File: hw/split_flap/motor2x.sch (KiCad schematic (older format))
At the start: 5 parts, among them J10 Conn_01x05, J9 Conn_01x05, U4 ULN2803A, U9 74HC595

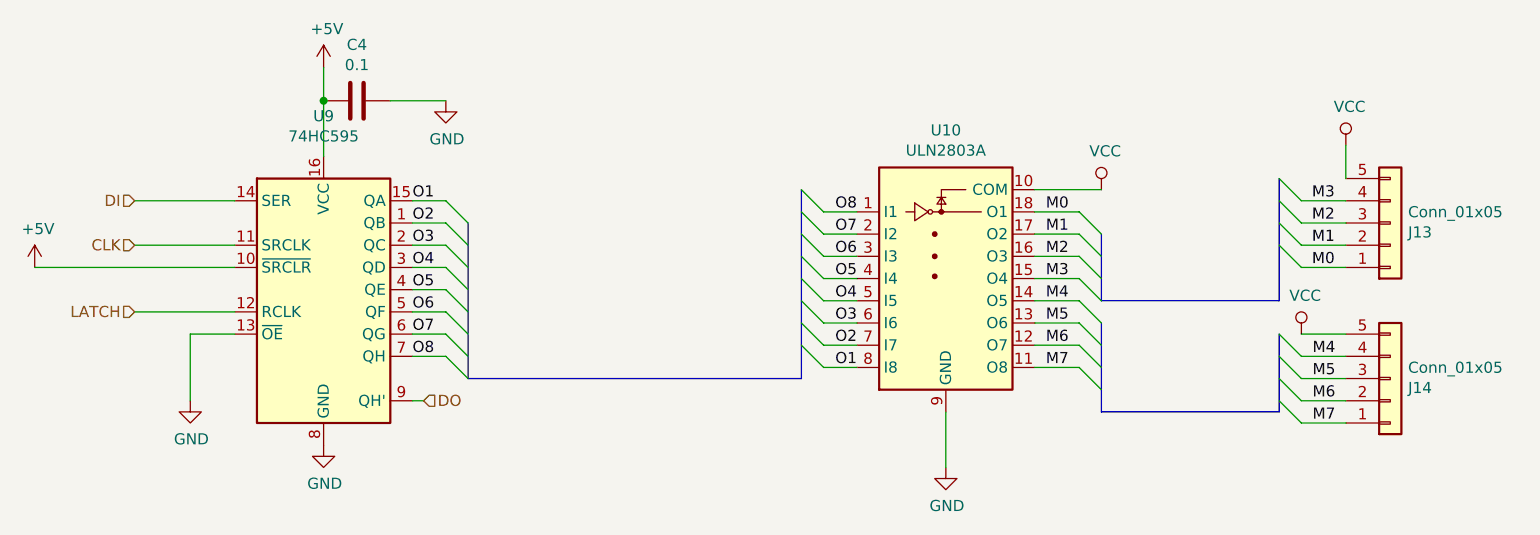
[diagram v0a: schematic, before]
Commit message: Add i2c pullups
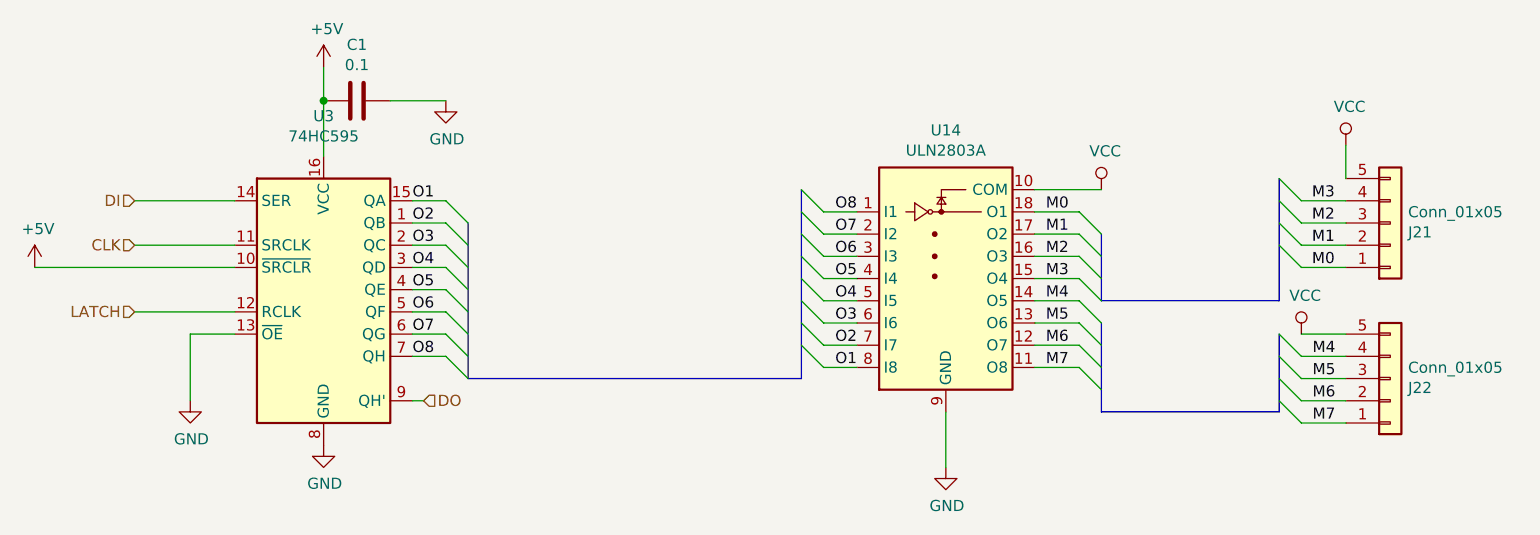
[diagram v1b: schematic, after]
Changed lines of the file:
@@
 AR Path="/5E0964A4/5E0DEDAF" Ref="#PWR033"  Part="1"
 AR Path="/5E0B21A0/5E0DEDAF" Ref="#PWR051"  Part="1"
-F 0 "#PWR051" H 4850 3850 50  0001 C CNN
+F 0 "#PWR0159" H 4850 3850 50  0001 C CNN
 F 1 "GND" H 4855 3927 50  0000 C CNN
 F 2 "" H 4850 4100 50  0001 C CNN
@@
 AR Path="/5E0964A4/5DF98B62" Ref="#PWR032"  Part="1"
 AR Path="/5E0B21A0/5DF98B62" Ref="#PWR050"  Part="1"
-F 0 "#PWR050" H 4850 2250 50  0001 C CNN
+F 0 "#PWR012" H 4850 2250 50  0001 C CNN
 F 1 "+5V" H 4865 2573 50  0000 C CNN
 F 2 "" H 4850 2400 50  0001 C CNN
@@
 AR Path="/5E0964A4/5DF9B643" Ref="#PWR031"  Part="1"
 AR Path="/5E0B21A0/5DF9B643" Ref="#PWR049"  Part="1"
-F 0 "#PWR049" H 4250 3650 50  0001 C CNN
+F 0 "#PWR011" H 4250 3650 50  0001 C CNN
 F 1 "GND" H 4255 3727 50  0000 C CNN
 F 2 "" H 4250 3900 50  0001 C CNN
@@
 AR Path="/5E0964A4/5DF9D02C" Ref="#PWR030"  Part="1"
 AR Path="/5E0B21A0/5DF9D02C" Ref="#PWR048"  Part="1"
-F 0 "#PWR048" H 3550 3150 50  0001 C CNN
+F 0 "#PWR08" H 3550 3150 50  0001 C CNN
 F 1 "+5V" H 3565 3473 50  0000 C CNN
 F 2 "" H 3550 3300 50  0001 C CNN
@@
 AR Path="/5E092C79/5E0E710C" Ref="C3"  Part="1"
 AR Path="/5E0B21A0/5E0E710C" Ref="C4"  Part="1"
-F 0 "C4" V 5252 2550 50  0000 C CNN
+F 0 "C1" V 5252 2550 50  0000 C CNN
 F 1 "0.1" V 5161 2550 50  0000 C CNN
 F 2 "Capacitor_THT:C_Disc_D4.3mm_W1.9mm_P5.00mm" H 5038 2400 50  0001 C CNN
@@
 AR Path="/5E0964A4/5E0E7881" Ref="#PWR034"  Part="1"
 AR Path="/5E0B21A0/5E0E7881" Ref="#PWR052"  Part="1"
-F 0 "#PWR052" H 5400 2300 50  0001 C CNN
+F 0 "#PWR013" H 5400 2300 50  0001 C CNN
 F 1 "GND" H 5405 2377 50  0000 C CNN
 F 2 "" H 5400 2550 50  0001 C CNN
@@
 AR Path="/5E0964A4/5DF4397F" Ref="U5"  Part="1"
 AR Path="/5E092C79/5DF4397F" Ref="U7"  Part="1"
-F 0 "U9" H 4850 4181 50  0000 C CNN
+F 0 "U3" H 4850 4181 50  0000 C CNN
 F 1 "74HC595" H 4850 4090 50  0000 C CNN
 F 2 "Package_SO:SOP-16_4.55x10.3mm_P1.27mm" H 4850 3400 50  0001 C CNN
@@
 AR Path="/5E0964A4/5E0DED94" Ref="J10"  Part="1"
 AR Path="/5E0B21A0/5E0DED94" Ref="J14"  Part="1"
-F 0 "J14" H 9730 3842 50  0000 L CNN
+F 0 "J22" H 9730 3842 50  0000 L CNN
 F 1 "Conn_01x05" H 9730 3751 50  0000 L CNN
 F 2 "Connector_JST:JST_XH_B5B-XH-A_1x05_P2.50mm_Vertical" H 9650 3800 50  0001 C CNN
@@
 AR Path="/5E0964A4/5E0DEDB5" Ref="#PWR035"  Part="1"
 AR Path="/5E0B21A0/5E0DEDB5" Ref="#PWR053"  Part="1"
-F 0 "#PWR053" H 7650 3950 50  0001 C CNN
+F 0 "#PWR0160" H 7650 3950 50  0001 C CNN
 F 1 "GND" H 7655 4027 50  0000 C CNN
 F 2 "" H 7650 4200 50  0001 C CNN
@@
 AR Path="/5E0964A4/5E0DEDBB" Ref="J9"  Part="1"
 AR Path="/5E0B21A0/5E0DEDBB" Ref="J13"  Part="1"
-F 0 "J13" H 9730 3142 50  0000 L CNN
+F 0 "J21" H 9730 3142 50  0000 L CNN
 F 1 "Conn_01x05" H 9730 3051 50  0000 L CNN
 F 2 "Connector_JST:JST_XH_B5B-XH-A_1x05_P2.50mm_Vertical" H 9650 3100 50  0001 C CNN
@@
 AR Path="/5E0964A4/5E0DEDCB" Ref="U6"  Part="1"
 AR Path="/5E0B21A0/5E0DEDCB" Ref="U10"  Part="1"
-F 0 "U10" H 7650 3817 50  0000 C CNN
+F 0 "U14" H 7650 3817 50  0000 C CNN
 F 1 "ULN2803A" H 7650 3726 50  0000 C CNN
 F 2 "Package_SO:SOP-18_7x12.5mm_P1.27mm" H 7700 2600 50  0001 L CNN
@@
 AR Path="/5E0964A4/5DF9DFD8" Ref="#PWR047"  Part="1"
 AR Path="/5E0B21A0/5DF9DFD8" Ref="#PWR057"  Part="1"
-F 0 "#PWR057" H 8350 2800 50  0001 C CNN
+F 0 "#PWR045" H 8350 2800 50  0001 C CNN
 F 1 "VCC" H 8367 3123 50  0000 C CNN
 F 2 "" H 8350 2950 50  0001 C CNN
@@
 AR Path="/5E0964A4/5DF9E5BE" Ref="#PWR054"  Part="1"
 AR Path="/5E0B21A0/5DF9E5BE" Ref="#PWR058"  Part="1"
-F 0 "#PWR058" H 9450 2600 50  0001 C CNN
+F 0 "#PWR046" H 9450 2600 50  0001 C CNN
 F 1 "VCC" H 9467 2923 50  0000 C CNN
 F 2 "" H 9450 2750 50  0001 C CNN
@@
 AR Path="/5E0964A4/5DFA3442" Ref="#PWR068"  Part="1"
 AR Path="/5E0B21A0/5DFA3442" Ref="#PWR070"  Part="1"
-F 0 "#PWR070" H 9250 3450 50  0001 C CNN
+F 0 "#PWR059" H 9250 3450 50  0001 C CNN
 F 1 "VCC" H 9267 3773 50  0000 C CNN
 F 2 "" H 9250 3600 50  0001 C CNN
